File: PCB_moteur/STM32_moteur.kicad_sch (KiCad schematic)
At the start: 31 parts, among them J1 RFD900, J8 CAM, U1 STM32F103CBT6, Y1 16mhz

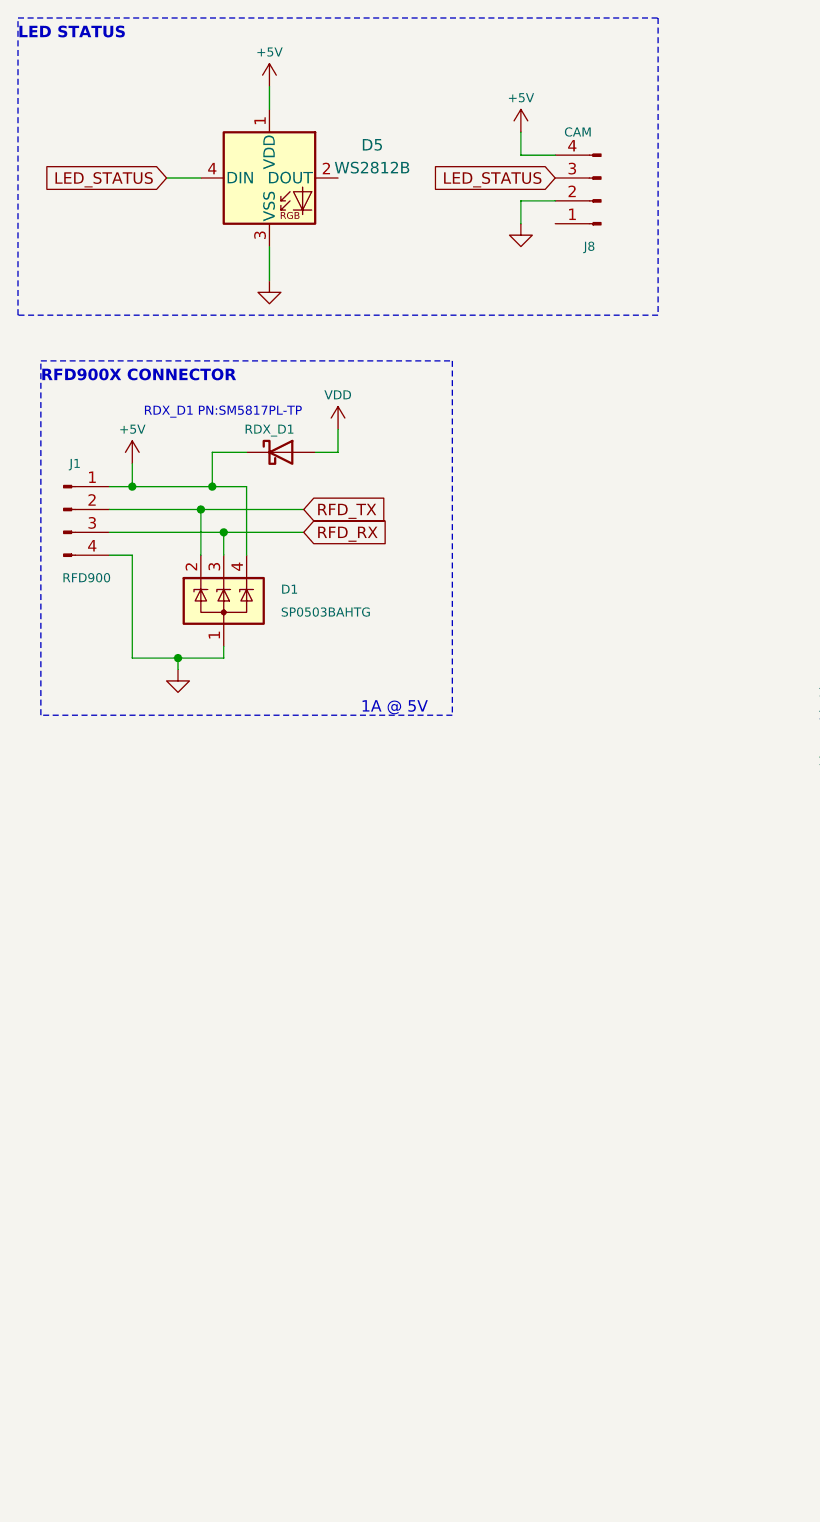
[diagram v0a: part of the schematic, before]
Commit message: Manque supply, pyro et finition (découplage etc)
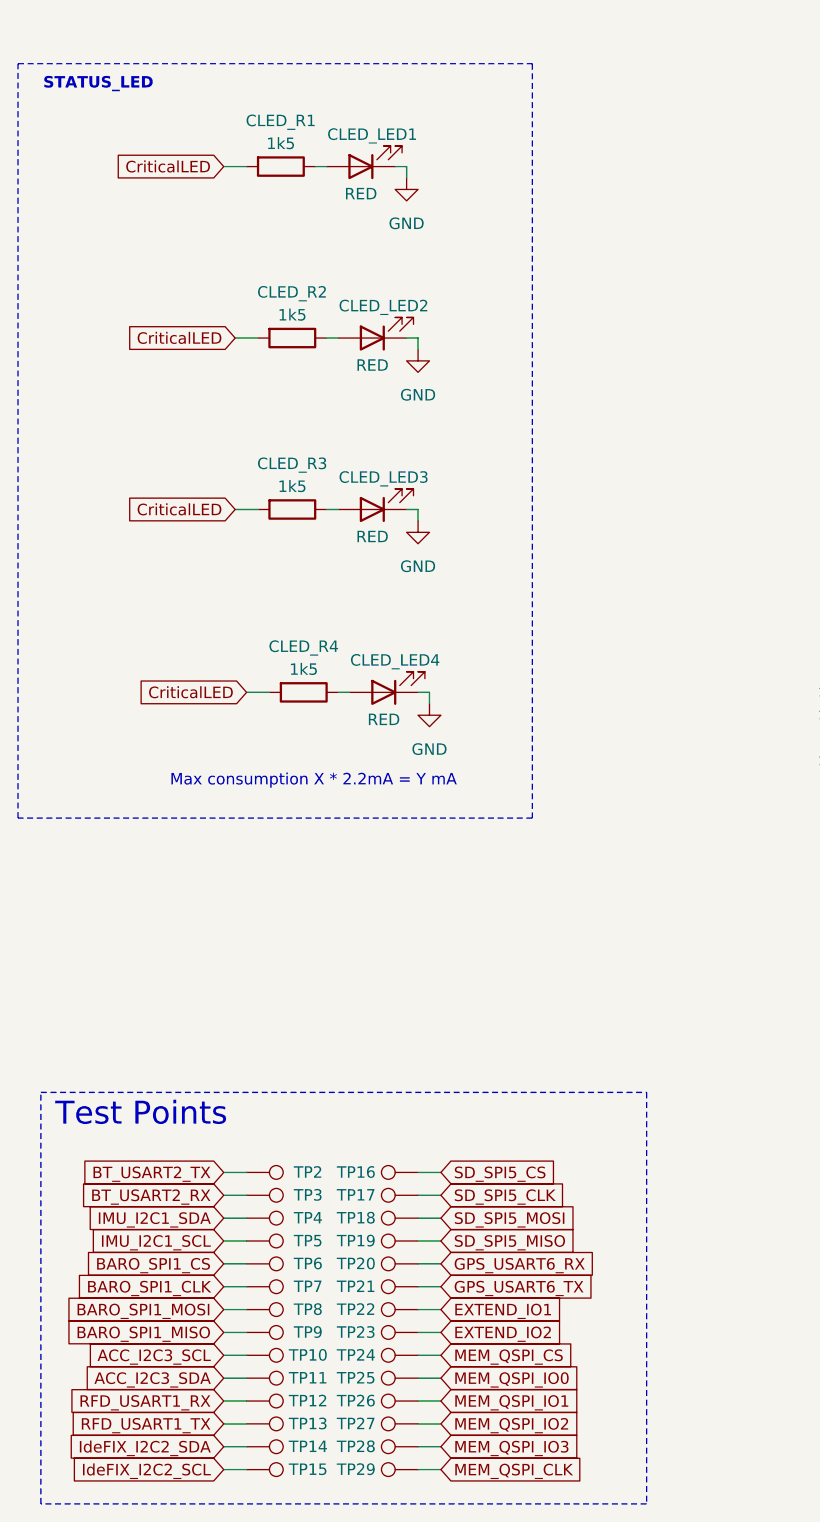
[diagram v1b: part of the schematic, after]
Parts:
- removed D1: SP0503BAHTG, Package_TO_SOT_SMD:SOT-143, symbol Power_Protection:SP0503BAHT
- removed D5: WS2812B, LED_SMD:LED_WS2812B_PLCC4_5.0x5.0mm_P3.2mm, symbol LED:WS2812B
- removed J1: RFD900, custom_footprints:B4B-PH-K, symbol Connector:Conn_01x04_Pin
- removed J8: CAM, custom_footprints:B4B-PH-K, symbol Connector:Conn_01x04_Pin
- removed RDX_D1: B260A-13-F, Diode_SMD:D_SOD-123, symbol Device:D_Schottky
- added CLED_LED1, CLED_LED2, CLED_LED3, CLED_LED4: RED, LED_SMD:LED_0603_1608Metric, symbol Device:LED
- added CLED_R1, CLED_R2, CLED_R3, CLED_R4: 1k5, Resistor_SMD:R_0603_1608Metric, symbol Device:R
- added TP10, TP11, TP12, TP13, TP14, TP15, TP16, TP17, TP18, TP19, TP2, TP20, TP21, TP22, TP23, TP24, TP25, TP26, TP27, TP28, TP29, TP3, TP4, TP5, TP6, TP7, TP8, TP9: TestPoint, TestPoint:TestPoint_Pad_D1.0mm, symbol Connector:TestPoint
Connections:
- net GND: now also CLED_LED1.1 (K), CLED_LED2.1 (K), CLED_LED3.1 (K), CLED_LED4.1 (K)
- new net: CLED_LED1.2 (A), CLED_R1.1
- new net: CLED_LED3.2 (A), CLED_R3.1
- new net: CLED_LED4.2 (A), CLED_R4.1
- new net: CLED_LED2.2 (A), CLED_R2.1
- new net ACC_I2C3_SCL: TP10.1
- new net ACC_I2C3_SDA: TP11.1
- new net BARO_SPI1_CLK: TP7.1
- new net BARO_SPI1_CS: TP6.1
- new net BARO_SPI1_MISO: TP9.1
- new net BARO_SPI1_MOSI: TP8.1
- new net BT_USART2_RX: TP3.1
- new net BT_USART2_TX: TP2.1
- new net CriticalLED: CLED_R1.2, CLED_R2.2, CLED_R3.2, CLED_R4.2
- new net EXTEND_IO1: TP22.1
- new net EXTEND_IO2: TP23.1
- new net GPS_USART6_RX: TP20.1
- new net GPS_USART6_TX: TP21.1
- new net IMU_I2C1_SCL: TP5.1
- new net IMU_I2C1_SDA: TP4.1
- new net IdeFIX_I2C2_SCL: TP15.1
- new net IdeFIX_I2C2_SDA: TP14.1
- new net MEM_QSPI_CLK: TP29.1
- new net MEM_QSPI_CS: TP24.1
- new net MEM_QSPI_IO0: TP25.1
- new net MEM_QSPI_IO1: TP26.1
- new net MEM_QSPI_IO2: TP27.1
- new net MEM_QSPI_IO3: TP28.1
- new net RFD_USART1_RX: TP12.1
- new net RFD_USART1_TX: TP13.1
- new net SD_SPI5_CLK: TP17.1
- new net SD_SPI5_CS: TP16.1
- new net SD_SPI5_MISO: TP19.1
- new net SD_SPI5_MOSI: TP18.1
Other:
- note added: "Max consumption X * 2.2mA = Y mA"
- note added: "STATUS_LED"
- note added: "Test Points"
- note removed: "1A @ 5V"
- note removed: "LED STATUS"
- note removed: "RDX_D1 PN:SM5817PL-TP"
- note removed: "RFD900X CONNECTOR"

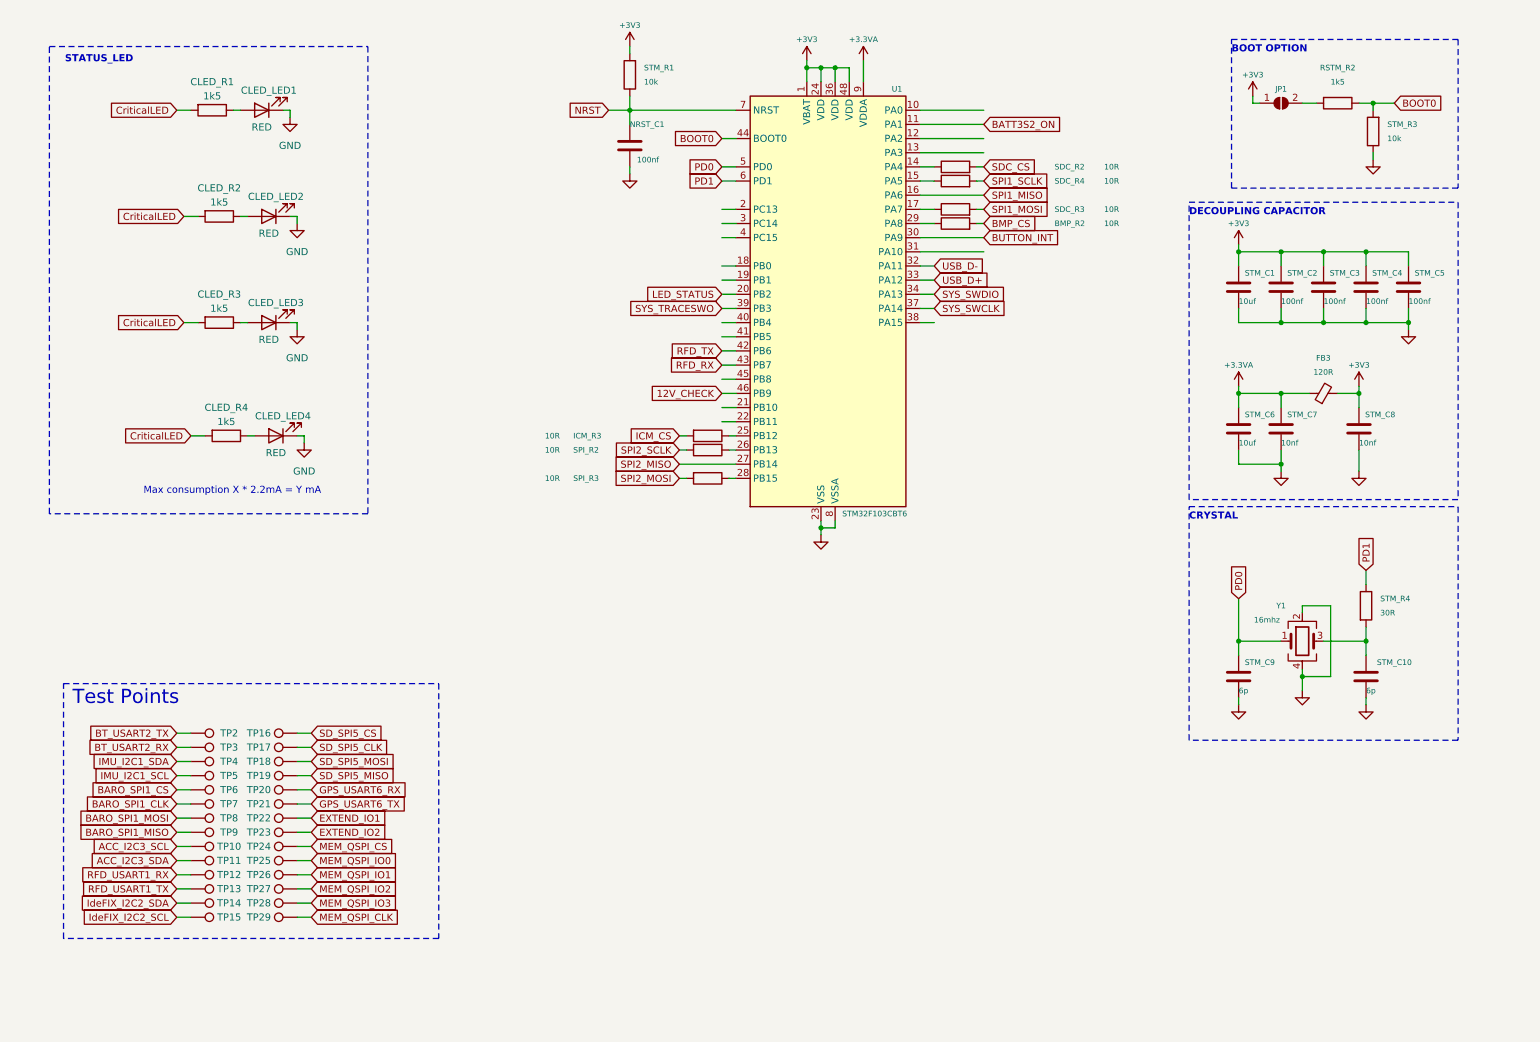
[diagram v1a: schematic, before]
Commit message: wip: remove unnecessary components
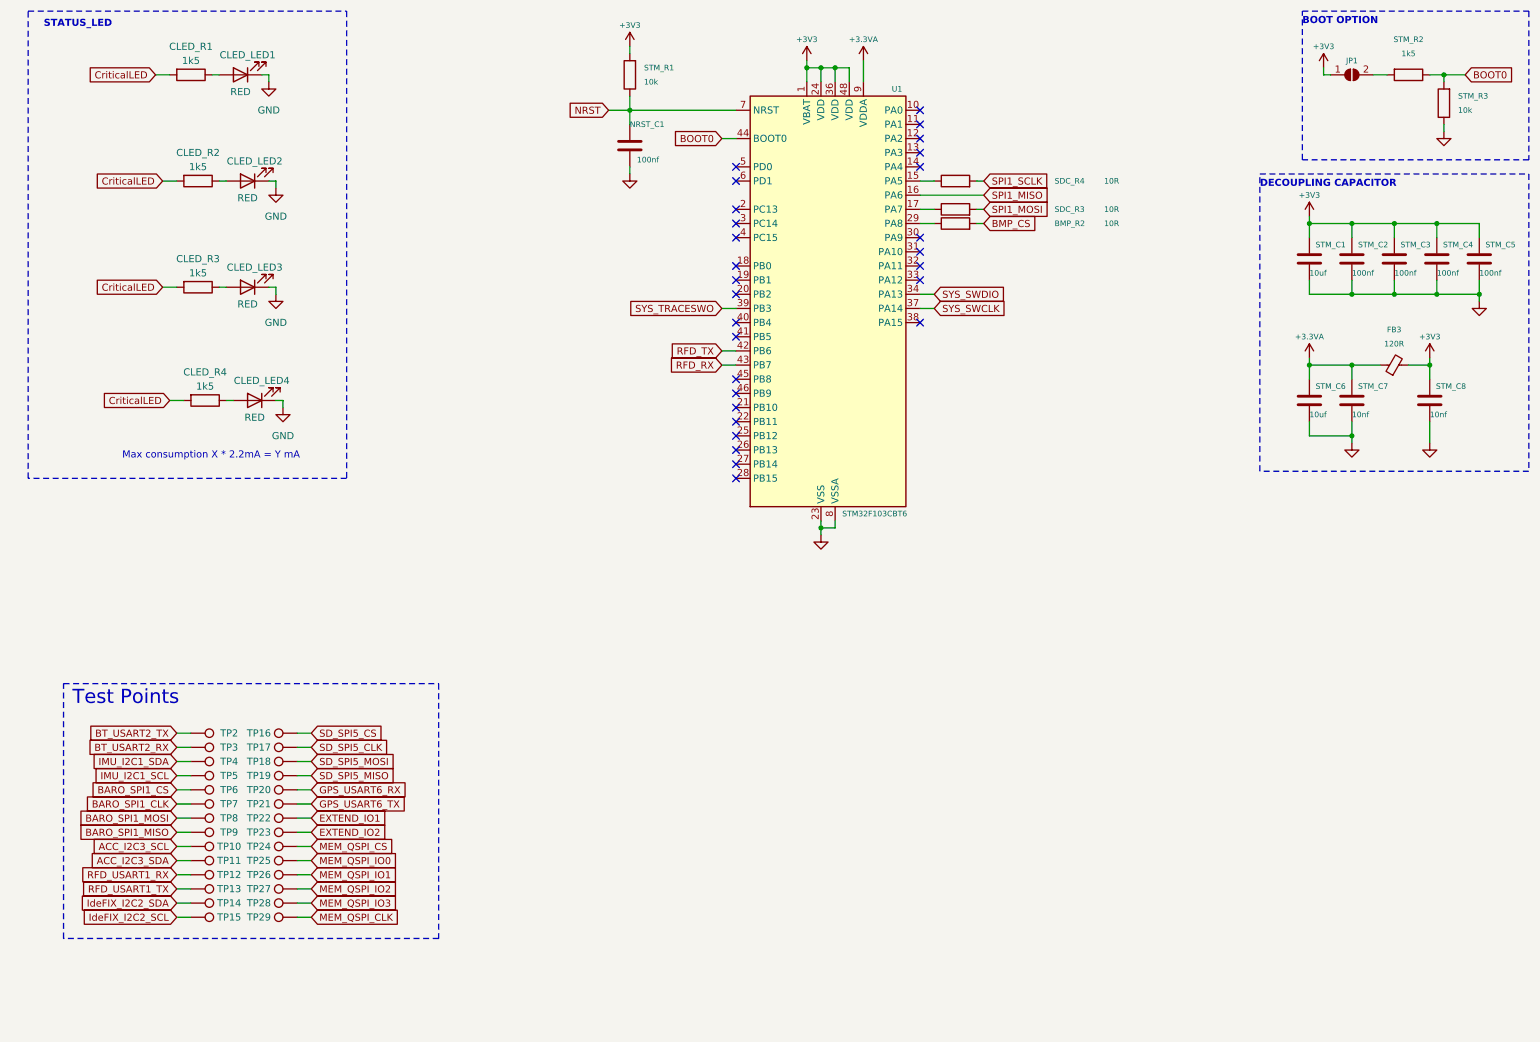
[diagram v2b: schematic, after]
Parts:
- removed ICM_R3, SDC_R2, SPI_R2, SPI_R3: 10R, Resistor_SMD:R_0805_2012Metric, symbol Device:R
- removed STM_C10, STM_C9: 6p, Capacitor_SMD:C_0805_2012Metric, symbol Device:C
- removed STM_R4: 30R, Resistor_SMD:R_0805_2012Metric, symbol Device:R
- removed Y1: 16mhz, Crystal:Crystal_SMD_3225-4Pin_3.2x2.5mm, symbol Device:Crystal_GND24
- renumbered RSTM_R2 to STM_R2
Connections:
- net 12V_CHECK: no longer names the net of U1.46 (PB9)
- net BATT3S2_ON: no longer names the net of U1.11 (PA1)
- net BUTTON_INT: no longer names the net of U1.30 (PA9)
- net LED_STATUS: no longer names the net of U1.20 (PB2)
- net PD0: no longer names the net of U1.5 (PD0)
- net PD1: no longer names the net of U1.6 (PD1)
- net SPI2_MISO: no longer names the net of U1.27 (PB14)
- net USB_D+: no longer names the net of U1.33 (PA12)
- net USB_D-: no longer names the net of U1.32 (PA11)
- no-connect marks 0 -> 28
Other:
- note removed: "CRYSTAL"
- moved on the sheet: CLED_LED1, CLED_LED2, CLED_LED3, CLED_LED4, CLED_R1, CLED_R2, CLED_R3, CLED_R4, FB3, JP1, STM_C1, STM_C2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
